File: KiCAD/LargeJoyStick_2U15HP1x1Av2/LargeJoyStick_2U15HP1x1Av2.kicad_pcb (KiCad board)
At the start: 2 copper layers, 75.9 x 84 mm, 5 parts

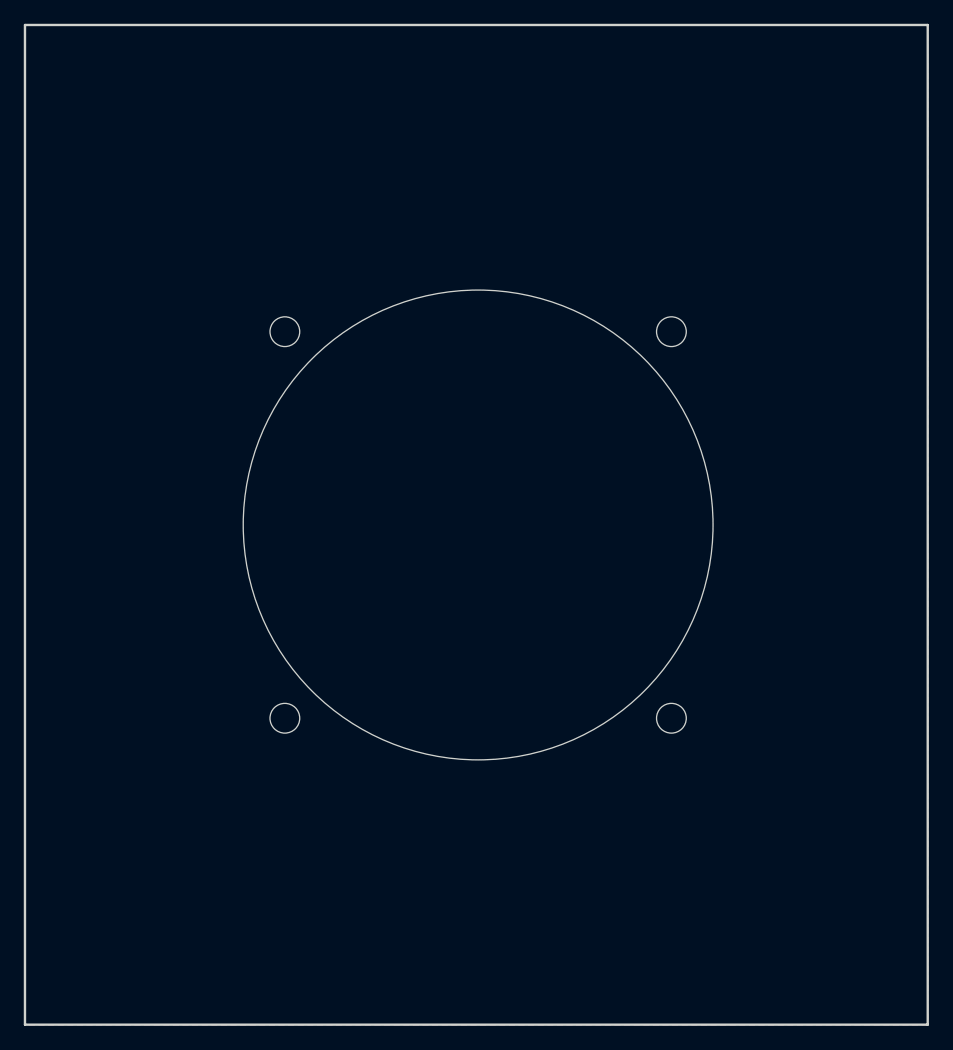
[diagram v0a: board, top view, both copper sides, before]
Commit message: updated all modules to use plated through-holes wherever possible
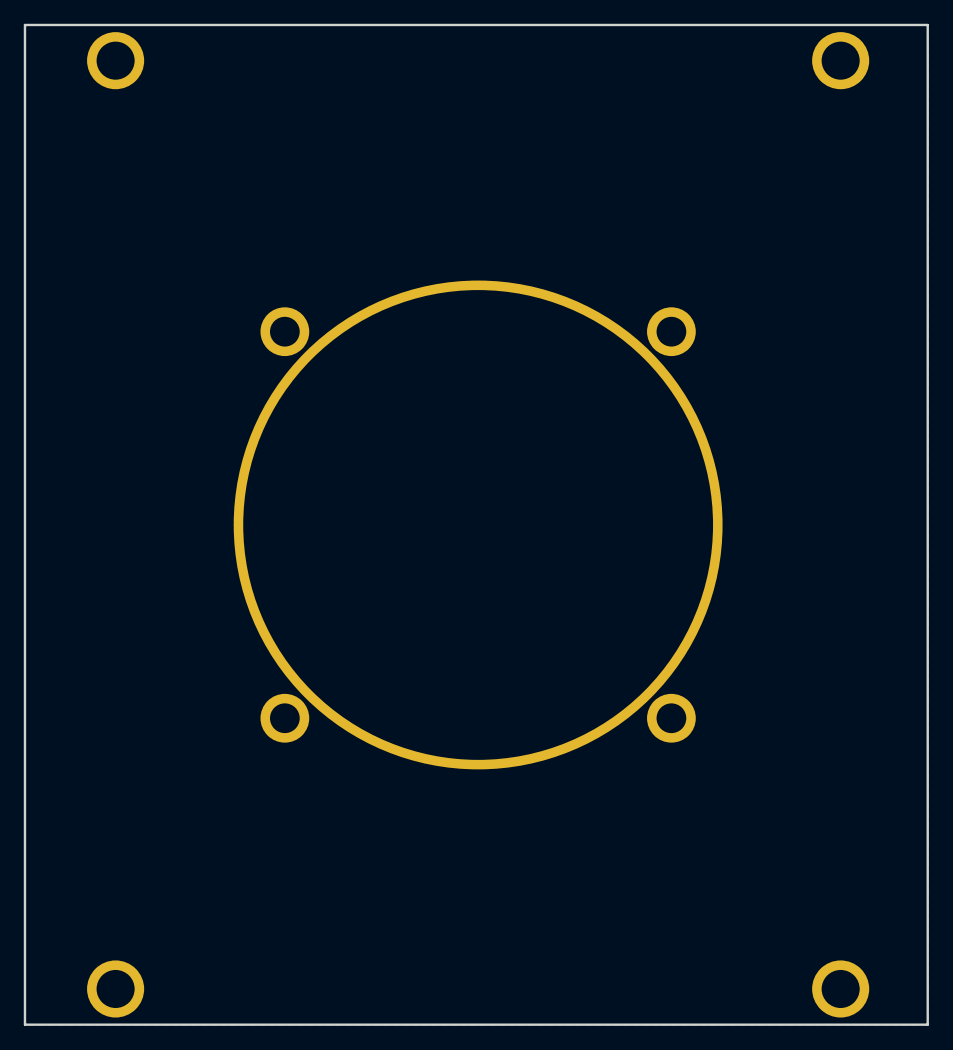
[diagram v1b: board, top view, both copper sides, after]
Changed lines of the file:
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@@
 			)
 		)
-		(pad "" np_thru_hole oval
+		(pad "" thru_hole circle
 			(at 0 0)
-			(size 4.34 3.2)
-			(drill oval 4.34 3.2)
-			(layers "*.Cu" "*.Mask")
+			(size 4.8 4.8)
+			(drill 3.2)
+			(layers "*.Cu" "*.Mask")
+			(remove_unused_layers no)
 		)
 		(embedded_fonts no)
@@
 			)
 		)
-		(pad "" np_thru_hole oval
+		(pad "" thru_hole circle
 			(at 0 0)
-			(size 4.34 3.2)
-			(drill oval 4.34 3.2)
-			(layers "*.Cu" "*.Mask")
+			(size 4.8 4.8)
+			(drill 3.2)
+			(layers "*.Cu" "*.Mask")
+			(remove_unused_layers no)
 		)
 		(embedded_fonts no)
@@
 			)
 		)
-		(pad "" np_thru_hole oval
+		(pad "" thru_hole circle
 			(at 0 0)
-			(size 4.34 3.2)
-			(drill oval 4.34 3.2)
-			(layers "*.Cu" "*.Mask")
+			(size 4.8 4.8)
+			(drill 3.2)
+			(layers "*.Cu" "*.Mask")
+			(remove_unused_layers no)
 		)
 		(embedded_fonts no)
@@
 		(at 38.1 44.4625)
 		(property "Reference" "LJS1"
-			(at 0 -20.828 0)
+			(at -0.1 -21.4625 0)
 			(unlocked yes)
 			(layer "B.SilkS")
@@
 		)
 		(property "Value" "Analog_Joystick_M39_Panel_Mount"
-			(at 0 20.955 0)
+			(at 0 21.2875 0)
 			(unlocked yes)
 			(layer "F.Fab")
@@
 		)
 		(fp_text user "${REFERENCE}"
-			(at 0 -20.828 0)
-			(unlocked yes)
-			(layer "F.Fab")
-			(effects
-				(font
-					(size 1 1)
-					(thickness 0.15)
-				)
-			)
-		)
-		(pad "" np_thru_hole circle
+			(at 0 -21.4625 0)
+			(unlocked yes)
+			(layer "F.Fab")
+			(effects
+				(font
+					(size 1 1)
+					(thickness 0.15)
+				)
+			)
+		)
+		(pad "" thru_hole circle
 			(at -16.25 -16.25)
-			(size 2.5 2.5)
+			(size 4.1 4.1)
 			(drill 2.5)
 			(layers "*.Cu" "*.Mask")
-		)
-		(pad "" np_thru_hole circle
+			(remove_unused_layers no)
+		)
+		(pad "" thru_hole circle
 			(at -16.25 16.25)
-			(size 2.5 2.5)
+			(size 4.1 4.1)
 			(drill 2.5)
 			(layers "*.Cu" "*.Mask")
-		)
-		(pad "" np_thru_hole circle
+			(remove_unused_layers no)
+		)
+		(pad "" thru_hole circle
 			(at 0 0)
-			(size 39.5 39.5)
+			(size 41.1 41.1)
 			(drill 39.5)
 			(layers "*.Cu" "*.Mask")
-		)
-		(pad "" np_thru_hole circle
+			(remove_unused_layers no)
+		)
+		(pad "" thru_hole circle
 			(at 16.25 -16.25)
-			(size 2.5 2.5)
+			(size 4.1 4.1)
 			(drill 2.5)
 			(layers "*.Cu" "*.Mask")
-		)
-		(pad "" np_thru_hole circle
+			(remove_unused_layers no)
+		)
+		(pad "" thru_hole circle
 			(at 16.25 16.25)
-			(size 2.5 2.5)
+			(size 4.1 4.1)
 			(drill 2.5)
 			(layers "*.Cu" "*.Mask")
+			(remove_unused_layers no)
 		)
 		(embedded_fonts no)
@@
 			)
 		)
-		(pad "" np_thru_hole oval
+		(pad "" thru_hole circle
 			(at 0 0)
-			(size 4.34 3.2)
-			(drill oval 4.34 3.2)
-			(layers "*.Cu" "*.Mask")
+			(size 4.8 4.8)
+			(drill 3.2)
+			(layers "*.Cu" "*.Mask")
+			(remove_unused_layers no)
 		)
 		(embedded_fonts no)
